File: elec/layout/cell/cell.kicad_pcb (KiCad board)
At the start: 4 copper layers, 79.5 x 8 mm, 64 parts

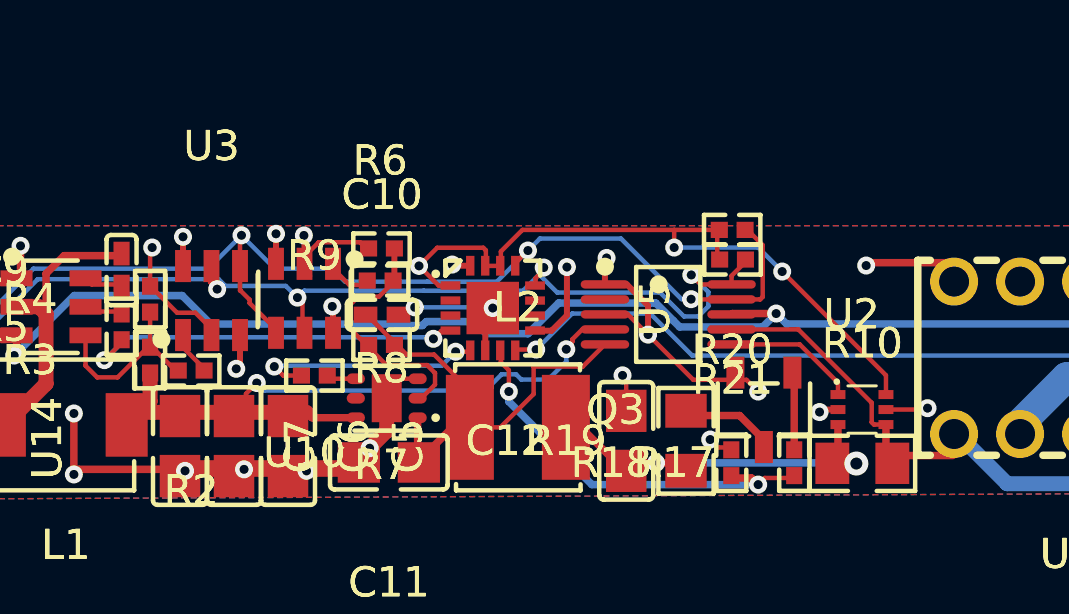
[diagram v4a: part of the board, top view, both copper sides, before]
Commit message: Fix addressor issues and layout relinking
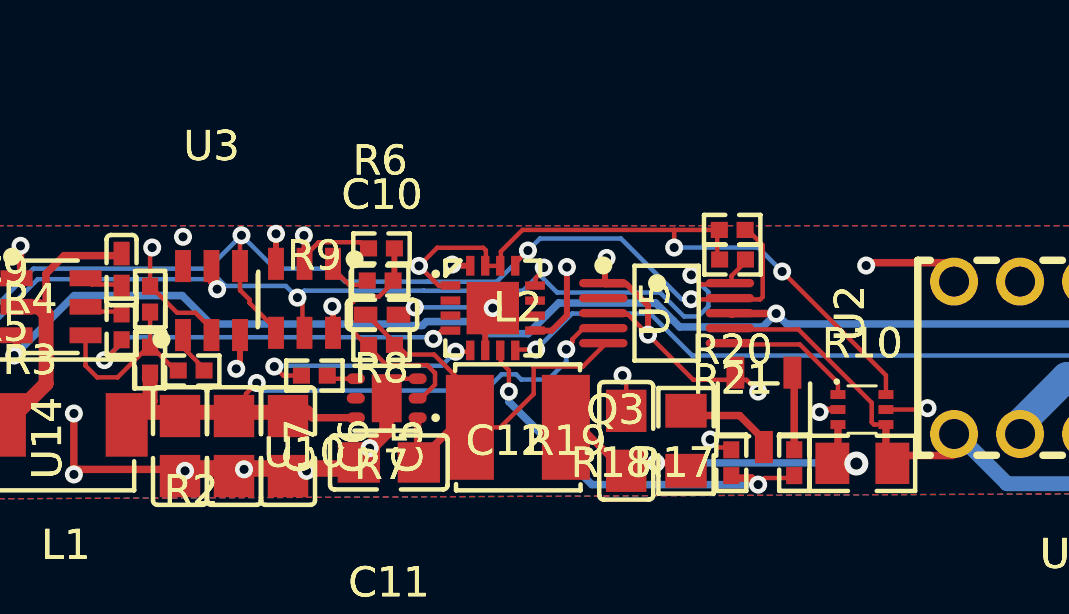
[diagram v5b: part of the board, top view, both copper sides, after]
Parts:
- R1, R11, R14: value 2.2kΩ ±1% 62.5mW -> 2kΩ ±1% 62.5mW
- R3: value 36.5kΩ ±1% 62.5mW -> 37.4kΩ ±1% 62.5mW
- moved U2 0.07 mm to (148.9, 103.8)
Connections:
- net adc-line renamed ALERT
- C1 pad 1: hv-5 -> hv-4
- C1 pad 2: gnd-4 -> gnd-2
- C10 pad 2: gnd-5 -> 3V3_GND
- C11 pad 2: gnd-5 -> 3V3_GND
- C12 pad 1: hv-4 -> hv-5
- C12 pad 2: gnd-5 -> 3V3_GND
- C13 pad 1: hv-8 -> hv-1
- C13 pad 2: gnd-1 -> gnd-3
- C14 pad 1: hv-8 -> hv-1
- C14 pad 2: gnd-1 -> gnd-3
- C15 pad 2: gnd-5 -> 3V3_GND
- C16 pad 2: gnd-5 -> 3V3_GND
- C2 pad 2: gnd-5 -> 3V3_GND
- C3 pad 2: gnd-5 -> 3V3_GND
- C4 pad 2: gnd-5 -> 3V3_GND
- C5 pad 2: gnd-5 -> 3V3_GND
- C6 pad 2: gnd-5 -> 3V3_GND
- C7 pad 2: gnd-5 -> 3V3_GND
- L2 pad 2: hv-4 -> hv-5
- LED3 pad 2: hv-8 -> hv-1
- Q1 pad 2: gnd-5 -> 3V3_GND
- Q2 pad 2: gnd-1 -> gnd-3
- Q3 pad 2: gnd-5 -> 3V3_GND
- Q3 pad 3: gnd-3 -> gnd-5
- Q4 pad 2: gnd-5 -> 3V3_GND
- Q4 pad 3: gnd-6 -> gnd-4
- R10 pad 1: hv-4 -> hv-5
- R10 pad 2: hv-6 -> hv-9
- R11 pad 2: gnd-5 -> 3V3_GND
- R13 pad 2: gnd-5 -> 3V3_GND
- R15 pad 1: line-1 -> line-3
- R16 pad 1: line-1 -> line-3
- R16 pad 2: gnd-1 -> gnd-3
- R17 pad 1: line-7 -> line-5
- R18 pad 1: line-7 -> line-5
- R18 pad 2: gnd-5 -> 3V3_GND
- R19 pad 1: hv-4 -> hv-5
- R19 pad 2: gnd-3 -> gnd-5
- R22 pad 1: line -> line-6
- R23 pad 1: line -> line-6
- R23 pad 2: gnd-5 -> 3V3_GND
- R24 pad 1: hv-3 -> hv-8
- R24 pad 2: hv-2 -> hv-6
- R25 pad 1: gnd-7 -> gnd-6
- R25 pad 2: gnd -> gnd-1
- R26 pad 1: hv-9 -> hv-3
- R26 pad 2: gnd-6 -> gnd-4
- R4 pad 2: gnd-5 -> 3V3_GND
- R5 pad 1: line-2 -> line-1
- R8 pad 2: gnd-5 -> 3V3_GND
- R9 pad 1: line-4 -> line-9
- U1 pad 1: hv-5 -> hv-4
- U1 pad 2: gnd-4 -> gnd-2
- U1 pad 4: gnd-5 -> 3V3_GND
- U10 pad 2: gnd-5 -> 3V3_GND
- U10 pad 6: gnd-5 -> 3V3_GND
- U11 pad 1: hv-1 -> hv-2
- U11 pad 2: line-3 -> line-2
- U11 pad 3: line-5 -> line
- U11 pad 4: gnd-2 -> gnd
- U11 pad 5: gnd-5 -> 3V3_GND
- U12 pad 1: hv-8 -> hv-1
- U12 pad 3: gnd-1 -> gnd-3
- U12 pad 4: line-6 -> line-4
- U13 pad 1: hv-8 -> hv-1
- U13 pad 2: line-6 -> line-4
- U13 pad 3: gnd-1 -> gnd-3
- U14 pad 1: gnd-5 -> 3V3_GND
- U2 pad 1: gnd-5 -> 3V3_GND
- U2 pad 3: gnd-5 -> 3V3_GND
- U2 pad 6: line-9 -> line-7
- U2 pad 7: hv-6 -> hv-9
- U3 pad 2: gnd-5 -> 3V3_GND
- U3 pad 6: 3V3 -> A0
- U4 pad 1: gnd-5 -> 3V3_GND
- U5 pad 10: gpio-line-1 -> gpio-line
- U5 pad 16: gnd-5 -> 3V3_GND
- U5 pad 17: gnd-5 -> 3V3_GND
- U5 pad 2: gpio-line-2 -> gpio-line-1
- U5 pad 3: line-2 -> line-1
- U5 pad 4: gpio-line -> gpio-line-2
- U5 pad 5: line-4 -> line-9
- U5 pad 6: gnd-5 -> 3V3_GND
- U5 pad 7: line-7 -> line-5
- U5 pad 9: line -> line-6
- U6 pad 3: gnd-5 -> 3V3_GND
- U6 pad 7: gnd-5 -> 3V3_GND
- U7 pad 1: line-9 -> line-7
- U7 pad 2: gnd-5 -> 3V3_GND
- U7 pad 3: hv-4 -> hv-5
- U7 pad 4: hv-6 -> hv-9
- U7 pad 5: gnd-5 -> 3V3_GND
- U8 pad 3: gnd-5 -> 3V3_GND
- U8 pad 4: gnd-5 -> 3V3_GND
- U8 pad 5: hv-6 -> hv-9
- U8 pad 6: hv-9 -> hv-3
- U9 pad 1: hv-8 -> hv-1
- U9 pad 3: gnd-7 -> gnd-6
- U9 pad 4: gnd-5 -> 3V3_GND
- U9 pad 5: hv-6 -> hv-9
- U9 pad 6: hv-3 -> hv-8
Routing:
- net 3V3_GND: track 0.00 -> 107.9 mm, vias 0 -> 33
- net gnd-5: track 107.9 -> 3.42 mm, vias 33 -> 0
- net line: track 31.7 -> 0.00 mm, vias 2 -> 0
- net line-6: track 2.29 -> 31.7 mm, vias 0 -> 2
- net hv-6: track 27.5 -> 0.00 mm, vias 1 -> 0
- net line-5: track 0.00 -> 13.5 mm, vias 0 -> 2
- net hv-9: track 14.3 -> 27.5 mm
- net line-2: track 12.8 -> 0.00 mm, vias 2 -> 0
- net hv-3: track 1.58 -> 14.3 mm, vias 0 -> 1
- net line-1: track 1.44 -> 12.8 mm, vias 0 -> 2
- net gnd-2: track 0.00 -> 10.8 mm, vias 0 -> 1
- net hv-1: track 0.00 -> 10.0 mm, vias 0 -> 1
- net line-7: track 13.5 -> 4.47 mm, vias 2 -> 0
- net gnd-4: track 10.8 -> 1.89 mm, vias 1 -> 0
- net hv-5: track 4.33 -> 13.2 mm, vias 0 -> 2
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- added copper zone on B.Cu, net 3V3_GND
- added copper zone on F.Cu, net 3V3_GND
- added copper zone on In2.Cu, net 3V3_GND
- added copper zone on In1.Cu, net A0
- removed copper zone on In1.Cu, net 3V3
- removed copper zone on B.Cu, net gnd-5
- removed copper zone on F.Cu, net gnd-5
- removed copper zone on In2.Cu, net gnd-5

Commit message: fix 8ch layout
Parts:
- moved R22 0.11 mm to (172.5, 100.9)
- moved R23 0.11 mm to (170.5, 100.9)
- moved U10 0.07 mm to (136.8, 103.3)
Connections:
- C1 pad 1: hv-4 -> hv
- C1 pad 2: gnd-2 -> gnd
- C10 pad 1: hv -> hv-9
- C11 pad 1: hv -> hv-9
- C12 pad 1: hv-5 -> hv-7
- C13 pad 1: hv-1 -> hv-3
- C13 pad 2: gnd-3 -> gnd-2
- C14 pad 1: hv-1 -> hv-3
- C14 pad 2: gnd-3 -> gnd-2
- C5 pad 1: hv-7 -> hv-6
- C6 pad 1: hv-7 -> hv-6
- C7 pad 1: hv-7 -> hv-6
- L1 pad 2: hv-7 -> hv-6
- L2 pad 1: hv -> hv-9
- L2 pad 2: hv-5 -> hv-7
- LED3 pad 2: hv-1 -> hv-3
- Q2 pad 2: gnd-3 -> gnd-2
- Q3 pad 3: gnd-5 -> gnd-1
- R10 pad 1: hv-5 -> hv-7
- R10 pad 2: hv-9 -> hv-2
- R12 pad 1: line-8 -> line-1
- R13 pad 1: line-8 -> line-1
- R15 pad 1: line-3 -> line-7
- R16 pad 1: line-3 -> line-7
- R16 pad 2: gnd-3 -> gnd-2
- R17 pad 1: line-5 -> line
- R18 pad 1: line-5 -> line
- R19 pad 1: hv-5 -> hv-7
- R19 pad 2: gnd-5 -> gnd-1
- R22 pad 1: line-6 -> line-4
- R23 pad 1: line-6 -> line-4
- R24 pad 1: hv-8 -> hv-1
- R24 pad 2: hv-6 -> hv-8
- R25 pad 1: gnd-6 -> gnd-5
- R25 pad 2: gnd-1 -> gnd-6
- R26 pad 1: hv-3 -> hv-5
- R3 pad 1: hv-7 -> hv-6
- R5 pad 1: line-1 -> line-8
- R7 pad 1: hv -> hv-9
- R9 pad 1: line-9 -> line-3
- U1 pad 1: hv-4 -> hv
- U1 pad 2: gnd-2 -> gnd
- U11 pad 1: hv-2 -> hv-4
- U11 pad 3: line -> line-6
- U11 pad 4: gnd -> gnd-3
- U12 pad 1: hv-1 -> hv-3
- U12 pad 3: gnd-3 -> gnd-2
- U12 pad 4: line-4 -> line-5
- U13 pad 1: hv-1 -> hv-3
- U13 pad 2: line-4 -> line-5
- U13 pad 3: gnd-3 -> gnd-2
- U2 pad 4: hv-7 -> hv-6
- U2 pad 5: hv -> hv-9
- U2 pad 6: line-7 -> line-9
- U2 pad 7: hv-9 -> hv-2
- U3 pad 6: A0 -> 3V3
- U5 pad 10: gpio-line -> gpio-line-1
- U5 pad 2: gpio-line-1 -> gpio-line
- U5 pad 3: line-1 -> gpio-line-2
- U5 pad 4: gpio-line-2 -> line-8
- U5 pad 5: line-9 -> line-3
- U5 pad 7: line-5 -> line
- U5 pad 8: line-8 -> line-1
- U5 pad 9: line-6 -> line-4
- U6 pad 1: hv -> hv-9
- U6 pad 6: hv-7 -> hv-6
- U7 pad 1: line-7 -> line-9
- U7 pad 3: hv-5 -> hv-7
- U7 pad 4: hv-9 -> hv-2
- U8 pad 5: hv-9 -> hv-2
- U8 pad 6: hv-3 -> hv-5
- U9 pad 1: hv-1 -> hv-3
- U9 pad 3: gnd-6 -> gnd-5
- U9 pad 5: hv-9 -> hv-2
- U9 pad 6: hv-8 -> hv-1
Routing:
- net line-6: track 31.7 -> 0.00 mm, vias 2 -> 0
- net line-4: track 2.29 -> 31.7 mm, vias 0 -> 2
- net hv-2: track 0.00 -> 27.5 mm, vias 0 -> 1
- net hv-6: track 0.00 -> 24.4 mm, vias 0 -> 2
- net line-8: track 30.4 -> 12.6 mm
- net line-1: track 12.8 -> 30.4 mm
- net line: track 0.00 -> 13.5 mm, vias 0 -> 2
- net hv-9: track 27.5 -> 15.6 mm, vias 1 -> 0
- net hv: track 15.6 -> 4.33 mm
- net line-5: track 13.5 -> 2.29 mm, vias 2 -> 0
- net hv-7: track 24.3 -> 13.2 mm
- net gnd: track 0.00 -> 10.8 mm, vias 0 -> 1
- net hv-1: track 10.0 -> 1.58 mm, vias 1 -> 0
- net line-3: track 1.44 -> 7.72 mm, vias 0 -> 2
- net gnd-2: track 10.8 -> 5.20 mm, vias 1 -> 6
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- added copper zone on In1.Cu, net 3V3
- removed copper zone on In1.Cu, net A0
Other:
- board outline removed

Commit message: questionable progress
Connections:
- C1 pad 1: hv -> hv-6
- C1 pad 2: gnd -> gnd-6
- C10 pad 1: hv-9 -> hv-5
- C11 pad 1: hv-9 -> hv-5
- C13 pad 1: hv-3 -> hv-4
- C13 pad 2: gnd-2 -> gnd
- C14 pad 1: hv-3 -> hv-4
- C14 pad 2: gnd-2 -> gnd
- C5 pad 1: hv-6 -> hv-2
- C6 pad 1: hv-6 -> hv-2
- C7 pad 1: hv-6 -> hv-2
- L1 pad 2: hv-6 -> hv-2
- L2 pad 1: hv-9 -> hv-5
- LED3 pad 2: hv-3 -> hv-4
- Q2 pad 2: gnd-2 -> gnd
- Q3 pad 3: gnd-1 -> gnd-2
- Q4 pad 3: gnd-4 -> gnd-5
- R10 pad 2: hv-2 -> hv-8
- R15 pad 1: line-7 -> line
- R16 pad 1: line-7 -> line
- R16 pad 2: gnd-2 -> gnd
- R17 pad 1: line -> line-4
- R18 pad 1: line -> line-4
- R19 pad 2: gnd-1 -> gnd-2
- R22 pad 1: line-4 -> line-3
- R23 pad 1: line-4 -> line-3
- R24 pad 2: hv-8 -> hv
- R25 pad 1: gnd-5 -> gnd-1
- R25 pad 2: gnd-6 -> gnd-4
- R26 pad 1: hv-5 -> hv-3
- R26 pad 2: gnd-4 -> gnd-5
- R3 pad 1: hv-6 -> hv-2
- R5 pad 1: line-8 -> line-7
- R7 pad 1: hv-9 -> hv-5
- R9 pad 1: line-3 -> line-5
- U1 pad 1: hv -> hv-6
- U1 pad 2: gnd -> gnd-6
- U11 pad 1: hv-4 -> vcc1
- U11 pad 2: line-2 -> sda1
- U11 pad 3: line-6 -> scl1
- U12 pad 1: hv-3 -> hv-4
- U12 pad 3: gnd-2 -> gnd
- U12 pad 4: line-5 -> line-6
- U13 pad 1: hv-3 -> hv-4
- U13 pad 2: line-5 -> line-6
- U13 pad 3: gnd-2 -> gnd
- U2 pad 4: hv-6 -> hv-2
- U2 pad 5: hv-9 -> hv-5
- U2 pad 6: line-9 -> line-2
- U2 pad 7: hv-2 -> hv-8
- U5 pad 10: gpio-line-1 -> gpio-line-2
- U5 pad 3: gpio-line-2 -> gpio-line-1
- U5 pad 4: line-8 -> line-7
- U5 pad 5: line-3 -> line-5
- U5 pad 7: line -> line-4
- U5 pad 9: line-4 -> line-3
- U6 pad 1: hv-9 -> hv-5
- U6 pad 6: hv-6 -> hv-2
- U7 pad 1: line-9 -> line-2
- U7 pad 4: hv-2 -> hv-8
- U8 pad 5: hv-2 -> hv-8
- U8 pad 6: hv-5 -> hv-3
- U9 pad 1: hv-3 -> hv-4
- U9 pad 3: gnd-5 -> gnd-1
- U9 pad 5: hv-2 -> hv-8
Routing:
- net hv-8: track 0.00 -> 27.5 mm, vias 0 -> 1
- net line-3: track 7.72 -> 31.7 mm
- net hv-6: track 24.4 -> 4.33 mm, vias 2 -> 0
- net line-4: track 31.7 -> 13.5 mm
- net hv-9: track 15.6 -> 0.00 mm
- net line-8: track 12.6 -> 0.00 mm, vias 2 -> 0
- net line: track 13.5 -> 1.44 mm, vias 2 -> 0
- net line-7: track 1.44 -> 12.6 mm, vias 0 -> 2
- net gnd-6: track 0.00 -> 10.8 mm, vias 0 -> 1
- net hv-4: track 0.00 -> 10.0 mm, vias 0 -> 1
- net gnd: track 10.8 -> 5.20 mm, vias 1 -> 6
- net line-5: track 2.29 -> 7.72 mm, vias 0 -> 2
- net line-9: track 4.47 -> 0.00 mm
- net line-2: track 0.00 -> 4.47 mm
- net hv: track 4.33 -> 0.00 mm
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
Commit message: cellsim8ch building, big cleanup
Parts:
- C1: value 2.2µF ±10% 50V X5R -> 2.2µF ±10% 25V X7R
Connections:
- C1 pad 1: hv-6 -> hv
- C1 pad 2: gnd-6 -> gnd-4
- C10 pad 1: hv-5 -> hv-1
- C11 pad 1: hv-5 -> hv-1
- C12 pad 1: hv-7 -> hv-3
- C13 pad 1: hv-4 -> hv-8
- C13 pad 2: gnd -> gnd-3
- C14 pad 1: hv-4 -> hv-8
- C14 pad 2: gnd -> gnd-3
- L2 pad 1: hv-5 -> hv-1
- L2 pad 2: hv-7 -> hv-3
- LED3 pad 2: hv-4 -> hv-8
- Q2 pad 2: gnd -> gnd-3
- Q3 pad 3: gnd-2 -> gnd-5
- Q4 pad 3: gnd-5 -> gnd-2
- R10 pad 1: hv-7 -> hv-3
- R10 pad 2: hv-8 -> hv-7
- R12 pad 1: line-1 -> line-4
- R13 pad 1: line-1 -> line-4
- R15 pad 1: line -> line-3
- R16 pad 1: line -> line-3
- R16 pad 2: gnd -> gnd-3
- R17 pad 1: line-4 -> line-2
- R18 pad 1: line-4 -> line-2
- R19 pad 1: hv-7 -> hv-3
- R19 pad 2: gnd-2 -> gnd-5
- R22 pad 1: line-3 -> line-7
- R23 pad 1: line-3 -> line-7
- R24 pad 1: hv-1 -> hv-5
- R24 pad 2: hv -> hv-4
- R25 pad 1: gnd-1 -> gnd
- R25 pad 2: gnd-4 -> gnd-1
- R26 pad 1: hv-3 -> hv-6
- R26 pad 2: gnd-5 -> gnd-2
- R5 pad 1: line-7 -> line
- R7 pad 1: hv-5 -> hv-1
- R9 pad 1: line-5 -> line-6
- U1 pad 1: hv-6 -> hv
- U1 pad 2: gnd-6 -> gnd-4
- U11 pad 4: gnd-3 -> gnd-6
- U12 pad 1: hv-4 -> hv-8
- U12 pad 3: gnd -> gnd-3
- U12 pad 4: line-6 -> line-1
- U13 pad 1: hv-4 -> hv-8
- U13 pad 2: line-6 -> line-1
- U13 pad 3: gnd -> gnd-3
- U2 pad 5: hv-5 -> hv-1
- U2 pad 6: line-2 -> line-5
- U2 pad 7: hv-8 -> hv-7
- U5 pad 4: line-7 -> line
- U5 pad 5: line-5 -> line-6
- U5 pad 7: line-4 -> line-2
- U5 pad 8: line-1 -> line-4
- U5 pad 9: line-3 -> line-7
- U6 pad 1: hv-5 -> hv-1
- U7 pad 1: line-2 -> line-5
- U7 pad 3: hv-7 -> hv-3
- U7 pad 4: hv-8 -> hv-7
- U8 pad 5: hv-8 -> hv-7
- U8 pad 6: hv-3 -> hv-6
- U9 pad 1: hv-4 -> hv-8
- U9 pad 3: gnd-1 -> gnd
- U9 pad 5: hv-8 -> hv-7
- U9 pad 6: hv-1 -> hv-5
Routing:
- net line-3: track 31.7 -> 1.44 mm, vias 2 -> 0
- net line-1: track 30.4 -> 2.29 mm, vias 2 -> 0
- net line-7: track 12.6 -> 31.7 mm
- net hv-8: track 27.5 -> 10.0 mm
- net line-4: track 13.5 -> 30.4 mm
- net hv-7: track 13.2 -> 27.5 mm, vias 2 -> 1
- net hv-5: track 15.6 -> 1.58 mm
- net hv-1: track 1.58 -> 15.6 mm
- net line: track 1.44 -> 12.6 mm, vias 0 -> 2
- net gnd-6: track 10.8 -> 0.00 mm, vias 1 -> 0
- net gnd-4: track 0.00 -> 10.8 mm, vias 0 -> 1
- net hv-4: track 10.0 -> 0.00 mm, vias 1 -> 0
- net hv-6: track 4.33 -> 14.3 mm, vias 0 -> 1
- net line-2: track 4.47 -> 13.5 mm, vias 0 -> 2
- net line-6: track 2.29 -> 7.72 mm, vias 0 -> 2
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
